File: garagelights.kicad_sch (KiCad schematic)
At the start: 40 parts, among them J1 Samtec SSW-104-03-F-S-RA, J2 Samtec SSW-106-01-L-S, J3 Screw_Terminal_01x01, J4 Screw_Terminal_01x01, Q1 ZVN4206AV, Q2 ZVN4206AV, Q3 ZVN4206AV, U1 NE555P, U2 NE555P, U3 4013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

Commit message: Rev A: as submitted to Osh Park order #fmnAZ4b4
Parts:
- J2: value Samtec SSW-106-01-L-S -> Molex 901361106; footprint Library:SAMTEC_SSW-106-01-X-S -> Library:CONN_SDA-90136_V_06_MOL
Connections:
- net +12V: now also J2.1 (Pin_1); no longer J2.01 (Pin_1)
- net GND: now also J2.6 (Pin_6); no longer J2.06 (Pin_6)
- net at Q3.1 (D): now also J2.5 (Pin_5); no longer J2.05 (Pin_5)
- net at Q2.1 (D): now also J2.4 (Pin_4); no longer J2.04 (Pin_4)
- net at Q1.1 (D): now also J2.3 (Pin_3); no longer J2.03 (Pin_3)
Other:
- note added: "Adafruit #3492: HC-SR04 ultrasonic range finder"
- note removed: "HC-SR04 ultrasonic range finder"
- title: (none) -> Garage Lights
- moved on the sheet: D2, D3, Q2, R6
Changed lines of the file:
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@@
 	(generator_version "9.0")
 	(paper "USLetter")
-	(text "HC-SR04 ultrasonic range finder"
+	(title_block
+		(title "Garage Lights")
+		(rev "A")
+		(comment 4 "Firmware-free ultrasonic range finder")
+	)
+	(text "Adafruit #3492:\nHC-SR04 ultrasonic range finder"
 		(exclude_from_sim no)
-		(at 148.336 24.892 0)
+		(at 134.366 24.13 0)
 		(effects
 			(font
 				(size 1.27 1.27)
 			)
+			(justify left)
 		)
 	)
@@
 		)
 	)
-	(text "Adafruit #2993: Tower Light - \nRed Yellow Green Alert Light with Buzzer - 12VDC"
+	(text "Adafruit #2993: Tower Light - \nRed Yellow Green Alert Light\nwith Buzzer - 12VDC"
 		(exclude_from_sim no)
-		(at 240.792 25.4 0)
+		(at 236.22 26.416 0)
 		(effects
 			(font
 				(size 1.27 1.27)
 			)
+			(justify left)
 		)
 	)
@@
 	)
 	(junction
-		(at 213.36 104.14)
+		(at 213.36 96.52)
 		(diameter 0)
 		(color 0 0 0 0)
@@
 	)
 	(junction
-		(at 213.36 106.68)
+		(at 213.36 99.06)
 		(diameter 0)
 		(color 0 0 0 0)
@@
 	(wire
 		(pts
-			(xy 213.36 106.68) (xy 217.17 106.68)
+			(xy 213.36 99.06) (xy 217.17 99.06)
 		)
 		(stroke
@@
 	(wire
 		(pts
-			(xy 213.36 106.68) (xy 213.36 109.22)
+			(xy 213.36 99.06) (xy 213.36 101.6)
 		)
 		(stroke
@@
 	(wire
 		(pts
-			(xy 195.58 73.66) (xy 195.58 104.14)
+			(xy 195.58 73.66) (xy 195.58 96.52)
 		)
 		(stroke
@@
 	(wire
 		(pts
-			(xy 224.79 111.76) (xy 224.79 114.3)
+			(xy 224.79 104.14) (xy 224.79 106.68)
 		)
 		(stroke
@@
 	(wire
 		(pts
-			(xy 195.58 104.14) (xy 200.66 104.14)
+			(xy 195.58 96.52) (xy 200.66 96.52)
 		)
 		(stroke
@@
 	(wire
 		(pts
-			(xy 213.36 104.14) (xy 213.36 106.68)
+			(xy 213.36 96.52) (xy 213.36 99.06)
 		)
 		(stroke
@@
 	(wire
 		(pts
-			(xy 208.28 109.22) (xy 213.36 109.22)
+			(xy 208.28 101.6) (xy 213.36 101.6)
 		)
 		(stroke
@@
 	(wire
 		(pts
-			(xy 224.79 49.53) (xy 224.79 101.6)
+			(xy 224.79 49.53) (xy 224.79 93.98)
 		)
 		(stroke
@@
 	(wire
 		(pts
-			(xy 195.58 109.22) (xy 200.66 109.22)
+			(xy 195.58 101.6) (xy 200.66 101.6)
 		)
 		(stroke
@@
 	(wire
 		(pts
-			(xy 213.36 88.9) (xy 213.36 92.71)
+			(xy 213.36 81.28) (xy 213.36 85.09)
 		)
 		(stroke
@@
 	(wire
 		(pts
-			(xy 208.28 104.14) (xy 213.36 104.14)
+			(xy 208.28 96.52) (xy 213.36 96.52)
 		)
 		(stroke
@@
 	(wire
 		(pts
-			(xy 195.58 125.73) (xy 195.58 109.22)
+			(xy 195.58 125.73) (xy 195.58 101.6)
 		)
 		(stroke
@@
 	(wire
 		(pts
-			(xy 213.36 100.33) (xy 213.36 104.14)
+			(xy 213.36 92.71) (xy 213.36 96.52)
 		)
 		(stroke
@@
 	(symbol
 		(lib_id "power:+5V")
-		(at 213.36 88.9 0)
+		(at 213.36 81.28 0)
 		(unit 1)
 		(exclude_from_sim no)
@@
 		(dnp no)
 		(property "Reference" "#PWR020"
-			(at 213.36 92.71 0)
+			(at 213.36 85.09 0)
 			(effects
 				(font
@@
 		)
 		(property "Value" "+5V"
-			(at 216.408 87.122 0)
+			(at 216.408 79.502 0)
 			(effects
 				(font
@@
 		)
 		(property "Footprint" ""
-			(at 213.36 88.9 0)
+			(at 213.36 81.28 0)
 			(effects
 				(font
@@
 		)
 		(property "Datasheet" ""
-			(at 213.36 88.9 0)
+			(at 213.36 81.28 0)
 			(effects
 				(font
@@
 		)
 		(property "Description" "Power symbol creates a global label with name \"+5V\""
-			(at 213.36 88.9 0)
+			(at 213.36 81.28 0)
 			(effects
 				(font
@@
 	(symbol
 		(lib_id "Diode:1N914")
-		(at 204.47 109.22 0)
+		(at 204.47 101.6 0)
 		(mirror x)
 		(unit 1)
@@
 		(dnp no)
 		(property "Reference" "D3"
-			(at 204.47 115.57 0)
+			(at 204.47 107.95 0)
 			(effects
 				(font
@@
 		)
 		(property "Value" "1N914"
-			(at 204.47 113.03 0)
+			(at 204.47 105.41 0)
 			(effects
 				(font
@@
 		)
 		(property "Footprint" "Diode_THT:D_DO-35_SOD27_P7.62mm_Horizontal"
-			(at 204.47 104.775 0)
+			(at 204.47 97.155 0)
 			(effects
 				(font
@@
 		)
 		(property "Datasheet" "http://www.vishay.com/docs/85622/1n914.pdf"
-			(at 204.47 109.22 0)
+			(at 204.47 101.6 0)
 			(effects
 				(font
@@
 		)
 		(property "Description" "100V 0.3A Small Signal Fast Switching Diode, DO-35"
-			(at 204.47 109.22 0)
+			(at 204.47 101.6 0)
 			(effects
 				(font
@@
 		)
 		(property "Sim.Device" "D"
-			(at 204.47 109.22 0)
+			(at 204.47 101.6 0)
 			(effects
 				(font
@@
 		)
 		(property "Sim.Pins" "1=K 2=A"
-			(at 204.47 109.22 0)
+			(at 204.47 101.6 0)
 			(effects
 				(font
@@
 	(symbol
 		(lib_id "Transistor_FET_Other:Q_NMOS_Depletion_DGS")
-		(at 222.25 106.68 0)
+		(at 222.25 99.06 0)
 		(unit 1)
 		(exclude_from_sim no)
@@
 		(fields_autoplaced yes)
 		(property "Reference" "Q2"
-			(at 228.6 105.4099 0)
+			(at 228.6 97.7899 0)
 			(effects
 				(font
@@
 		)
 		(property "Value" "ZVN4206AV"
-			(at 228.6 107.9499 0)
+			(at 228.6 100.3299 0)
 			(effects
 				(font
@@
 		)
 		(property "Footprint" "Package_TO_SOT_THT:TO-92S"
-			(at 222.25 106.68 0)
+			(at 222.25 99.06 0)
 			(effects
 				(font
@@
 		)
 		(property "Datasheet" "~"
-			(at 222.25 106.68 0)
+			(at 222.25 99.06 0)
 			(effects
 				(font
@@
 		)
 		(property "Description" "Depletion-mode N-channel MOSFET, drain/gate/source"
-			(at 222.25 106.68 0)
+			(at 222.25 99.06 0)
 			(effects
 				(font
@@
 	(symbol
 		(lib_id "Device:R_US")
-		(at 213.36 96.52 0)
+		(at 213.36 88.9 0)
 		(unit 1)
 		(exclude_from_sim no)
@@
 		(fields_autoplaced yes)
 		(property "Reference" "R6"
-			(at 215.9 95.2499 0)
+			(at 215.9 87.6299 0)
 			(effects
 				(font
@@
 		)
 		(property "Value" "1k"
-			(at 215.9 97.7899 0)
+			(at 215.9 90.1699 0)
 			(effects
 				(font
@@
 		)
 		(property "Footprint" "Resistor_THT:R_Axial_DIN0204_L3.6mm_D1.6mm_P7.62mm_Horizontal"
-			(at 214.376 96.774 90)
+			(at 214.376 89.154 90)
 			(effects
 				(font
@@
 		)
 		(property "Datasheet" "~"
-			(at 213.36 96.52 0)
+			(at 213.36 88.9 0)
 			(effects
 				(font
@@
 		)
 		(property "Description" "Resistor, US symbol"
-			(at 213.36 96.52 0)
+			(at 213.36 88.9 0)
 			(effects
 				(font
@@
 	(symbol
 		(lib_id "power:GND")
-		(at 224.79 114.3 0)
+		(at 224.79 106.68 0)
 		(unit 1)
 		(exclude_from_sim no)
@@
 		(fields_autoplaced yes)
 		(property "Reference" "#PWR024"
-			(at 224.79 120.65 0)
+			(at 224.79 113.03 0)
 			(effects
 				(font
@@
 		)
 		(property "Value" "GND"
-			(at 224.79 119.38 0)
+			(at 224.79 111.76 0)
 			(effects
 				(font
@@
 		)
 		(property "Footprint" ""
-			(at 224.79 114.3 0)
+			(at 224.79 106.68 0)
 			(effects
 				(font
@@
 		)
 		(property "Datasheet" ""
-			(at 224.79 114.3 0)
+			(at 224.79 106.68 0)
 			(effects
 				(font
@@
 		)
 		(property "Description" "Power symbol creates a global label with name \"GND\" , ground"
-			(at 224.79 114.3 0)
+			(at 224.79 106.68 0)
 			(effects
 				(font
@@
 		(dnp no)
 		(property "Reference" "J1"
-			(at 134.874 41.148 0)
+			(at 134.874 27.686 0)
 			(effects
 				(font
@@
 		)
 		(property "Value" "Samtec SSW-104-03-F-S-RA"
-			(at 138.176 41.148 0)
+			(at 131.318 41.656 0)
 			(effects
 				(font
@@
 		(dnp no)
 		(property "Reference" "J2"
-			(at 255.27 46.9899 0)
+			(at 251.46 38.862 0)
 			(effects
 				(font
@@
 			)
 		)
-		(property "Value" "Samtec SSW-106-01-L-S"
-			(at 259.334 61.468 90)
+		(property "Value" "Molex 901361106"
+			(at 246.126 57.404 0)
 			(effects
 				(font
@@
 			)
 		)
-		(property "Footprint" "Library:SAMTEC_SSW-106-01-X-S"
+		(property "Footprint" "Library:CONN_SDA-90136_V_06_MOL"
 			(at 252.73 46.99 0)
 			(effects
@@
 			)
 		)
-		(pin "05"
+		(pin "4"
 		)
-		(pin "02"
+		(pin "1"
 		)
-		(pin "06"
+		(pin "5"
 		)
-		(pin "04"
+		(pin "3"
 		)
-		(pin "03"
+		(pin "2"
 		)
-		(pin "01"
+		(pin "6"
 		)
 		(instances
@@
 	(symbol
 		(lib_id "Diode:1N914")
-		(at 204.47 104.14 0)
+		(at 204.47 96.52 0)
 		(unit 1)
 		(exclude_from_sim no)
@@
 		(dnp no)
 		(property "Reference" "D2"
-			(at 204.47 97.79 0)
+			(at 204.47 90.17 0)
 			(effects
 				(font
@@
 		)
 		(property "Value" "1N914"
-			(at 204.47 100.33 0)
+			(at 204.47 92.71 0)
 			(effects
 				(font
@@
 		)
 		(property "Footprint" "Diode_THT:D_DO-35_SOD27_P7.62mm_Horizontal"
-			(at 204.47 108.585 0)
+			(at 204.47 100.965 0)
 			(effects
 				(font
@@
 		)
 		(property "Datasheet" "http://www.vishay.com/docs/85622/1n914.pdf"
-			(at 204.47 104.14 0)
+			(at 204.47 96.52 0)
 			(effects
 				(font
@@
 		)
 		(property "Description" "100V 0.3A Small Signal Fast Switching Diode, DO-35"
-			(at 204.47 104.14 0)
+			(at 204.47 96.52 0)
 			(effects
 				(font
@@
 		)
 		(property "Sim.Device" "D"
-			(at 204.47 104.14 0)
+			(at 204.47 96.52 0)
 			(effects
 				(font
@@
 		)
 		(property "Sim.Pins" "1=K 2=A"
-			(at 204.47 104.14 0)
+			(at 204.47 96.52 0)
 			(effects
 				(font

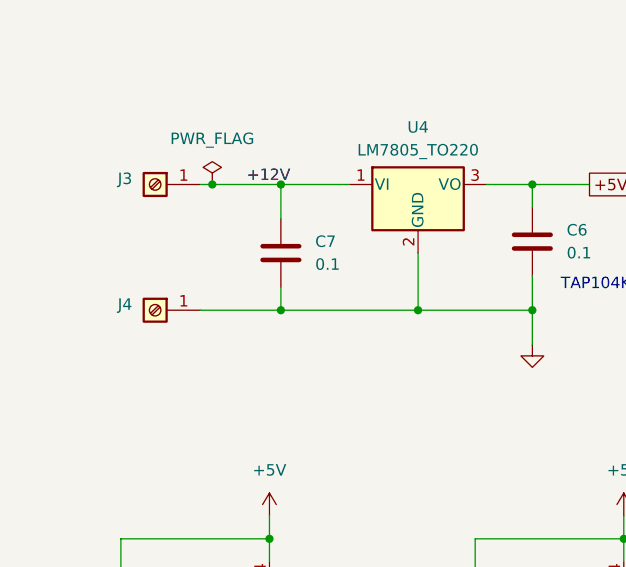
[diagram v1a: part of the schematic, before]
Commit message: Added a PWR_FLG and exclusion to clear ERCs
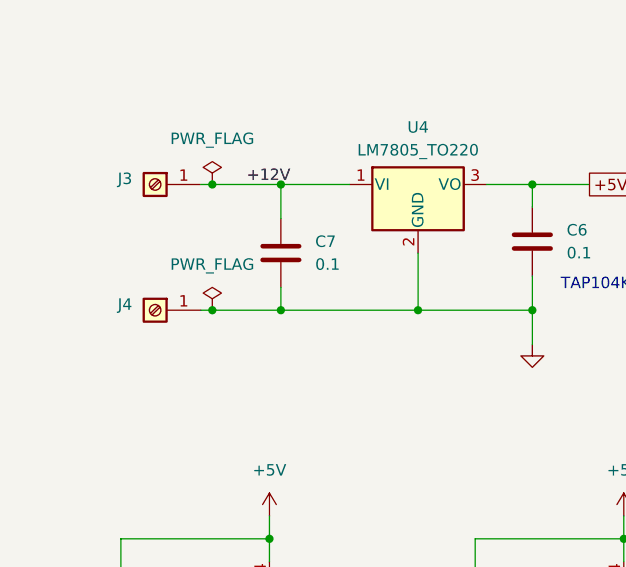
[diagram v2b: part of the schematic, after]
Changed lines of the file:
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@@
 	)
 	(junction
+		(at 44.45 139.7)
+		(diameter 0)
+		(color 0 0 0 0)
+	)
+	(junction
 		(at 52.07 139.7)
 		(diameter 0)
@@
 	(wire
 		(pts
+			(xy 44.45 139.7) (xy 52.07 139.7)
+		)
+		(stroke
+			(width 0)
+			(type default)
+		)
+	)
+	(wire
+		(pts
 			(xy 195.58 96.52) (xy 200.66 96.52)
 		)
@@
 	(wire
 		(pts
-			(xy 43.18 139.7) (xy 52.07 139.7)
+			(xy 43.18 139.7) (xy 44.45 139.7)
 		)
 		(stroke
@@
 					(unit 1)
 				)
+			)
+		)
+	)
+	(symbol
+		(lib_id "power:PWR_FLAG")
+		(at 44.45 139.7 0)
+		(unit 1)
+		(exclude_from_sim no)
+		(in_bom yes)
+		(on_board yes)
+		(dnp no)
+		(fields_autoplaced yes)
+		(property "Reference" "#FLG02"
+			(at 44.45 137.795 0)
+			(effects
+				(font
+					(size 1.27 1.27)
+				)
+				(hide yes)
+			)
+		)
+		(property "Value" "PWR_FLAG"
+			(at 44.45 134.62 0)
+			(effects
+				(font
+					(size 1.27 1.27)
+				)
+			)
+		)
+		(property "Footprint" ""
+			(at 44.45 139.7 0)
+			(effects
+				(font
+					(size 1.27 1.27)
+				)
+				(hide yes)
+			)
+		)
+		(property "Datasheet" "~"
+			(at 44.45 139.7 0)
+			(effects
+				(font
+					(size 1.27 1.27)
+				)
+				(hide yes)
+			)
+		)
+		(property "Description" "Special symbol for telling ERC where power comes from"
+			(at 44.45 139.7 0)
+			(effects
+				(font
+					(size 1.27 1.27)
+				)
+				(hide yes)
+			)
+		)
+		(pin "1"
+		)
+		(instances
+			(project "garagelights"
+				(path "/8304b3b7-1ae3-4935-a8ef-a9ab1b0a3004"
+					(reference "#FLG02")
+					(unit 1)
+				)

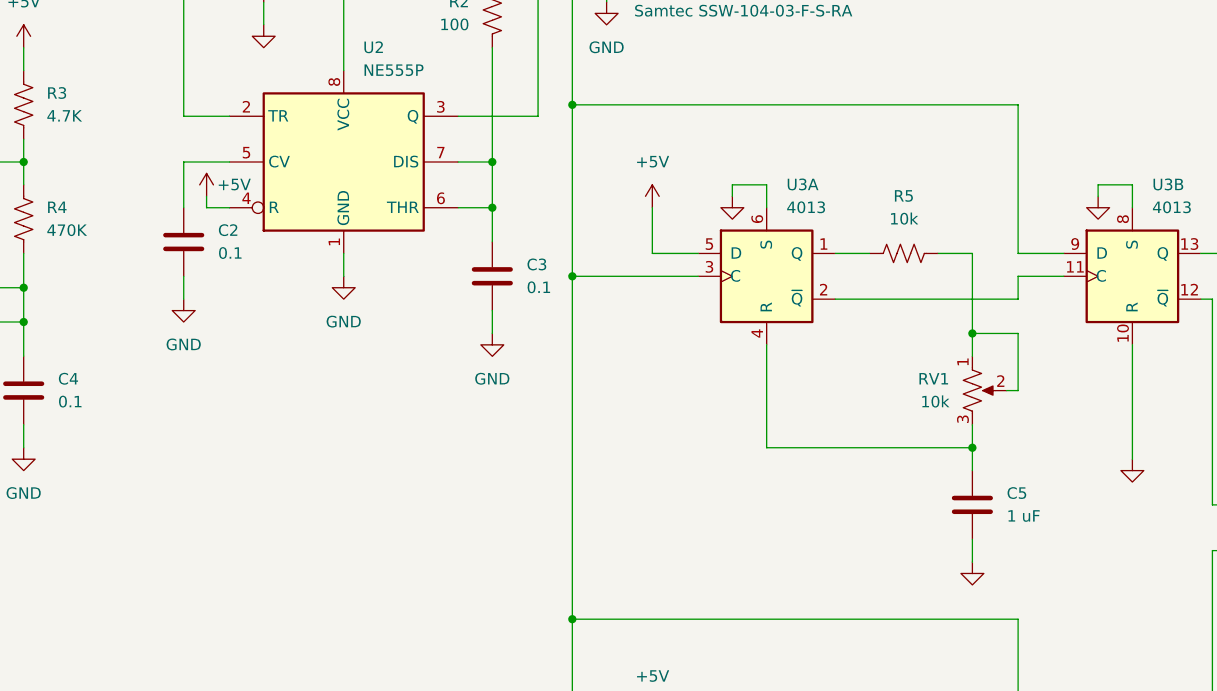
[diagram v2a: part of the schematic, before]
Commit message: Changed the timing capacitors: 1 uF ceramic C0G isn't a thing.
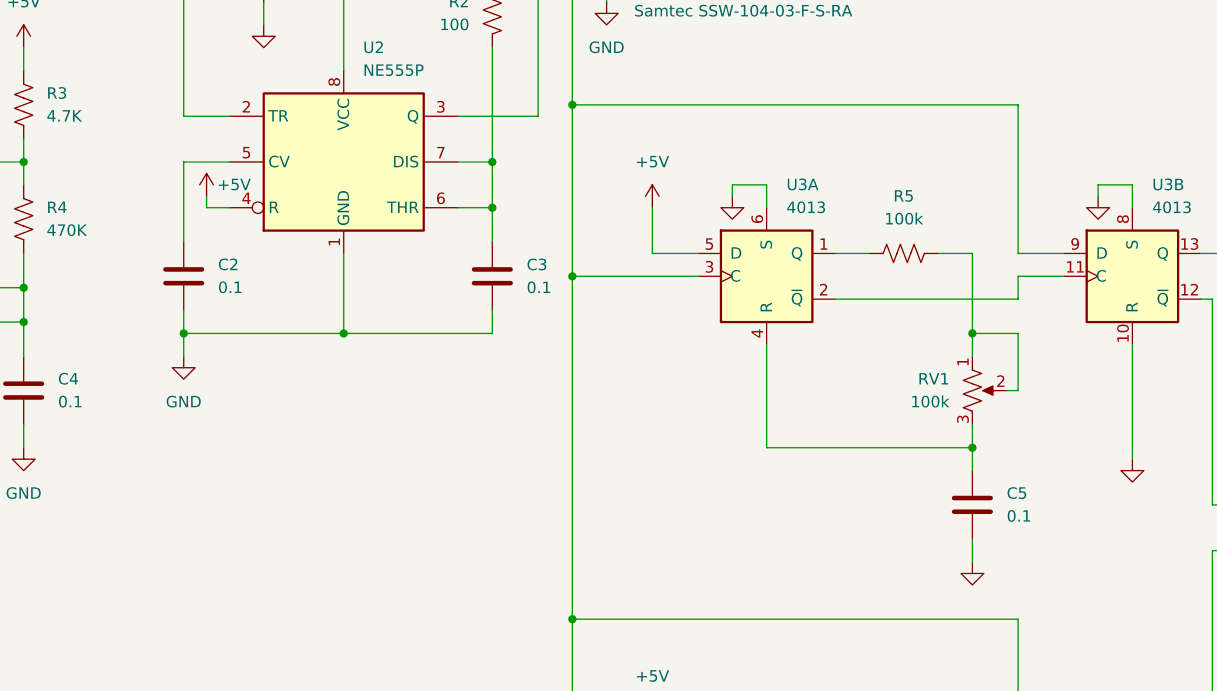
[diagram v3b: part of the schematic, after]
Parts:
- C5: value 1 uF -> 0.1
- H1, H2, H3, H4: now in the parts list
- R5, RV1: value 10k -> 100k
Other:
- moved on the sheet: C2
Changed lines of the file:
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@@
 	)
 	(junction
+		(at 81.28 77.47)
+		(diameter 0)
+		(color 0 0 0 0)
+	)
+	(junction
 		(at 124.46 109.22)
 		(diameter 0)
@@
 	)
 	(junction
+		(at 99.06 77.47)
+		(diameter 0)
+		(color 0 0 0 0)
+	)
+	(junction
 		(at 168.91 77.47)
 		(diameter 0)
@@
 	(wire
 		(pts
-			(xy 81.28 58.42) (xy 81.28 63.5)
+			(xy 81.28 58.42) (xy 81.28 67.31)
 		)
 		(stroke
@@
 	(wire
 		(pts
+			(xy 81.28 77.47) (xy 81.28 74.93)
+		)
+		(stroke
+			(width 0)
+			(type default)
+		)
+	)
+	(wire
+		(pts
 			(xy 173.99 83.82) (xy 173.99 77.47)
 		)
@@
 	(wire
 		(pts
-			(xy 81.28 73.66) (xy 81.28 71.12)
+			(xy 81.28 77.47) (xy 99.06 77.47)
+		)
+		(stroke
+			(width 0)
+			(type default)
+		)
+	)
+	(wire
+		(pts
+			(xy 81.28 80.01) (xy 81.28 77.47)
 		)
 		(stroke
@@
 	(wire
 		(pts
-			(xy 99.06 71.12) (xy 99.06 68.58)
+			(xy 99.06 77.47) (xy 99.06 68.58)
 		)
 		(stroke
@@
 	(wire
 		(pts
+			(xy 99.06 77.47) (xy 115.57 77.47)
+		)
+		(stroke
+			(width 0)
+			(type default)
+		)
+	)
+	(wire
+		(pts
 			(xy 90.17 40.64) (xy 90.17 43.18)
 		)
@@
 			)
 		)
-		(property "Value" "1 uF"
+		(property "Value" "0.1"
 			(at 172.72 97.7899 0)
 			(effects
@@
 		(unit 1)
 		(exclude_from_sim no)
-		(in_bom no)
+		(in_bom yes)
 		(on_board yes)
 		(dnp no)
@@
 	(symbol
 		(lib_id "power:GND")
-		(at 81.28 73.66 0)
+		(at 81.28 80.01 0)
 		(unit 1)
 		(exclude_from_sim no)
@@
 		(fields_autoplaced yes)
 		(property "Reference" "#PWR017"
-			(at 81.28 80.01 0)
+			(at 81.28 86.36 0)
 			(effects
 				(font
@@
 		)
 		(property "Value" "GND"
-			(at 81.28 78.74 0)
+			(at 81.28 85.09 0)
 			(effects
 				(font
@@
 		)
 		(property "Footprint" ""
-			(at 81.28 73.66 0)
+			(at 81.28 80.01 0)
 			(effects
 				(font
@@
 		)
 		(property "Datasheet" ""
-			(at 81.28 73.66 0)
+			(at 81.28 80.01 0)
 			(effects
 				(font
@@
 		)
 		(property "Description" "Power symbol creates a global label with name \"GND\" , ground"
-			(at 81.28 73.66 0)
+			(at 81.28 80.01 0)
 			(effects
 				(font
@@
 		(unit 1)
 		(exclude_from_sim no)
-		(in_bom no)
+		(in_bom yes)
 		(on_board yes)
 		(dnp no)
@@
 			)
 		)
-		(property "Value" "10k"
+		(property "Value" "100k"
 			(at 161.29 64.77 90)
 			(effects
@@
 			)
 		)
-		(property "Value" "10k"
+		(property "Value" "100k"
 			(at 166.37 85.0899 0)
 			(effects
@@
 	)
 	(symbol
-		(lib_id "power:GND")
-		(at 115.57 77.47 0)
-		(unit 1)
-		(exclude_from_sim no)
-		(in_bom yes)
-		(on_board yes)
-		(dnp no)
-		(fields_autoplaced yes)
-		(property "Reference" "#PWR018"
-			(at 115.57 83.82 0)
-			(effects
-				(font
-					(size 1.27 1.27)
-				)
-				(hide yes)
-			)
-		)
-		(property "Value" "GND"
-			(at 115.57 82.55 0)
-			(effects
-				(font
-					(size 1.27 1.27)
-				)
-			)
-		)
-		(property "Footprint" ""
-			(at 115.57 77.47 0)
-			(effects
-				(font
-					(size 1.27 1.27)
-				)
-				(hide yes)
-			)
-		)
-		(property "Datasheet" ""
-			(at 115.57 77.47 0)
-			(effects
-				(font
-					(size 1.27 1.27)
-				)
-				(hide yes)
-			)
-		)
-		(property "Description" "Power symbol creates a global label with name \"GND\" , ground"
-			(at 115.57 77.47 0)
-			(effects
-				(font
-					(size 1.27 1.27)
-				)
-				(hide yes)
-			)
-		)
-		(pin "1"
-		)
-		(instances
-			(project ""
-				(path "/8304b3b7-1ae3-4935-a8ef-a9ab1b0a3004"
-					(reference "#PWR018")
-					(unit 1)
-				)
-			)
-		)
-	)
-	(symbol
 		(lib_id "Device:C")
 		(at 63.5 83.82 0)
@@
 		(unit 1)
 		(exclude_from_sim no)
-		(in_bom no)
+		(in_bom yes)
 		(on_board yes)
 		(dnp no)
@@
 	)
 	(symbol
-		(lib_id "power:GND")
-		(at 99.06 71.12 0)
-		(unit 1)
-		(exclude_from_sim no)
-		(in_bom yes)
-		(on_board yes)
-		(dnp no)
-		(fields_autoplaced yes)
-		(property "Reference" "#PWR016"
-			(at 99.06 77.47 0)
-			(effects
-				(font
-					(size 1.27 1.27)
-				)
-				(hide yes)
-			)
-		)
-		(property "Value" "GND"
-			(at 99.06 76.2 0)
-			(effects
-				(font
-					(size 1.27 1.27)
-				)
-			)
-		)
-		(property "Footprint" ""
-			(at 99.06 71.12 0)
-			(effects
-				(font
-					(size 1.27 1.27)
-				)
-				(hide yes)
-			)
-		)
-		(property "Datasheet" ""
-			(at 99.06 71.12 0)
-			(effects
-				(font
-					(size 1.27 1.27)
-				)
-				(hide yes)
-			)
-		)
-		(property "Description" "Power symbol creates a global label with name \"GND\" , ground"
-			(at 99.06 71.12 0)
-			(effects
-				(font
-					(size 1.27 1.27)
-				)
-				(hide yes)
-			)
-		)
-		(pin "1"
-		)
-		(instances
-			(project ""
-				(path "/8304b3b7-1ae3-4935-a8ef-a9ab1b0a3004"
-					(reference "#PWR016")
-					(unit 1)
-				)
-			)
-		)
-	)
-	(symbol
 		(lib_id "Mechanical:MountingHole")
 		(at 115.57 162.56 0)
 		(unit 1)
 		(exclude_from_sim no)
-		(in_bom no)
+		(in_bom yes)
 		(on_board yes)
 		(dnp no)
@@
 	(symbol
 		(lib_id "Device:C")
-		(at 81.28 67.31 0)
+		(at 81.28 71.12 0)
 		(unit 1)
 		(exclude_from_sim no)
@@
 		(fields_autoplaced yes)
 		(property "Reference" "C2"
-			(at 85.09 66.0399 0)
+			(at 85.09 69.8499 0)
 			(effects
 				(font
@@
 		)
 		(property "Value" "0.1"
-			(at 85.09 68.5799 0)
+			(at 85.09 72.3899 0)
 			(effects
 				(font
@@
 		)
 		(property "Footprint" "Capacitor_THT:C_Disc_D5.0mm_W2.5mm_P2.50mm"
-			(at 82.2452 71.12 0)
+			(at 82.2452 74.93 0)
 			(effects
 				(font
@@
 		)
 		(property "Datasheet" "https://yageogroup.com/content/datasheet/asset/file/KEM_C1049_GOLDMAX_C0G"
-			(at 81.28 67.31 0)
+			(at 81.28 71.12 0)
 			(effects
 				(font
@@
 		)
 		(property "Description" "Unpolarized capacitor"
-			(at 81.28 67.31 0)
+			(at 81.28 71.12 0)
 			(effects
 				(font

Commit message: Update to KiCAD 10.0, replace J2 with 5-pin
J2 was 6-pin, but the ground pin was superfluous. The light tower
is switched on the low side, so there is no ground conductor.
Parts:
- J2: value Molex 901361106 -> Molex 705430004; footprint Library:CONN_SDA-90136_V_06_MOL -> Library:CONN_SDA-70543-xxxx_05_MOL; symbol Connector_Generic:Conn_01x06 -> Connector_Generic:Conn_01x05
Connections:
- net GND: no longer J2.6 (Pin_6)
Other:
- note added: "+12V"
- note added: "~{BUZZER}"
- note added: "~{GREEN}"
- note added: "~{RED}"
- note added: "~{YELLOW}"
- note removed: "GREEN"
- note removed: "RED"
- note removed: "YELLOW"
